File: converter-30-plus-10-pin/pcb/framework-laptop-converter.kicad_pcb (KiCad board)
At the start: 4 copper layers, 17.9 x 38 mm, 7 parts, among them J1 20879-040E-01, J2 FFC2B28-40-G

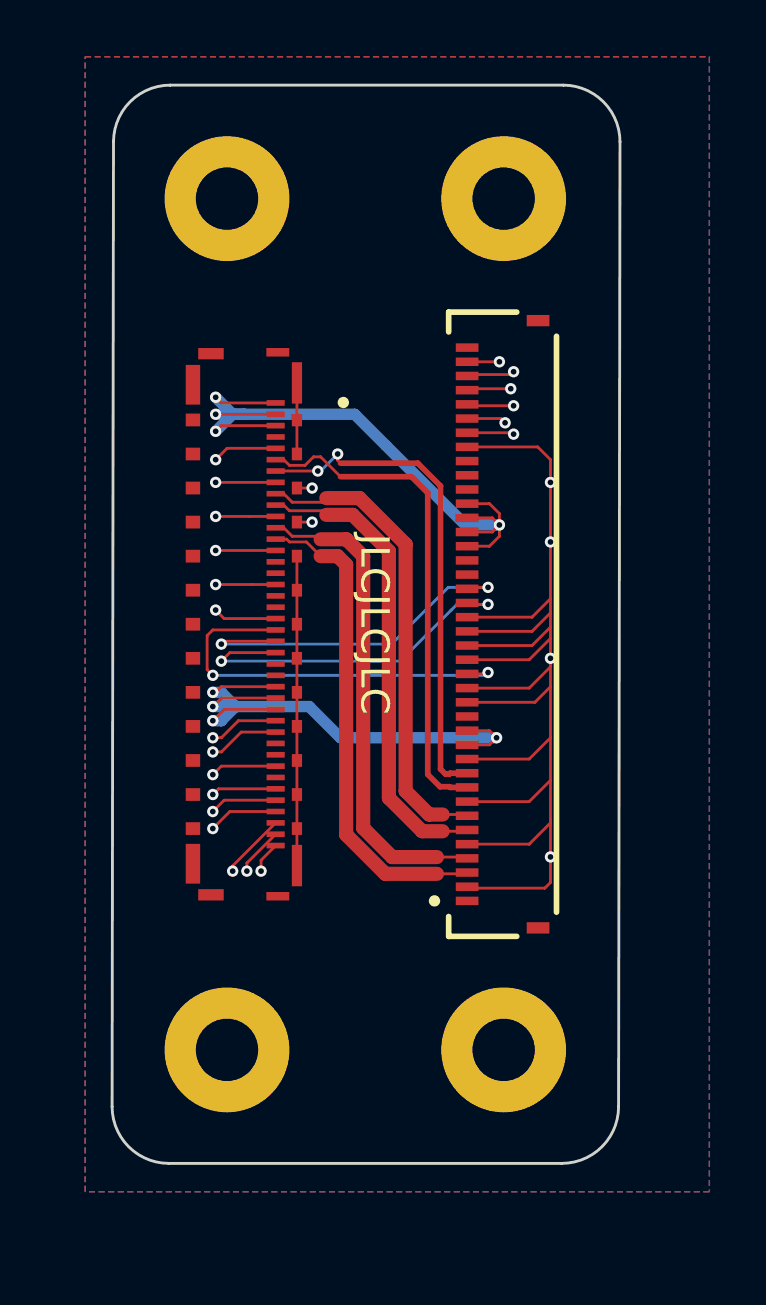
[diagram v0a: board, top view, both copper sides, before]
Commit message: fewer slots so this can be fabbed cheaper
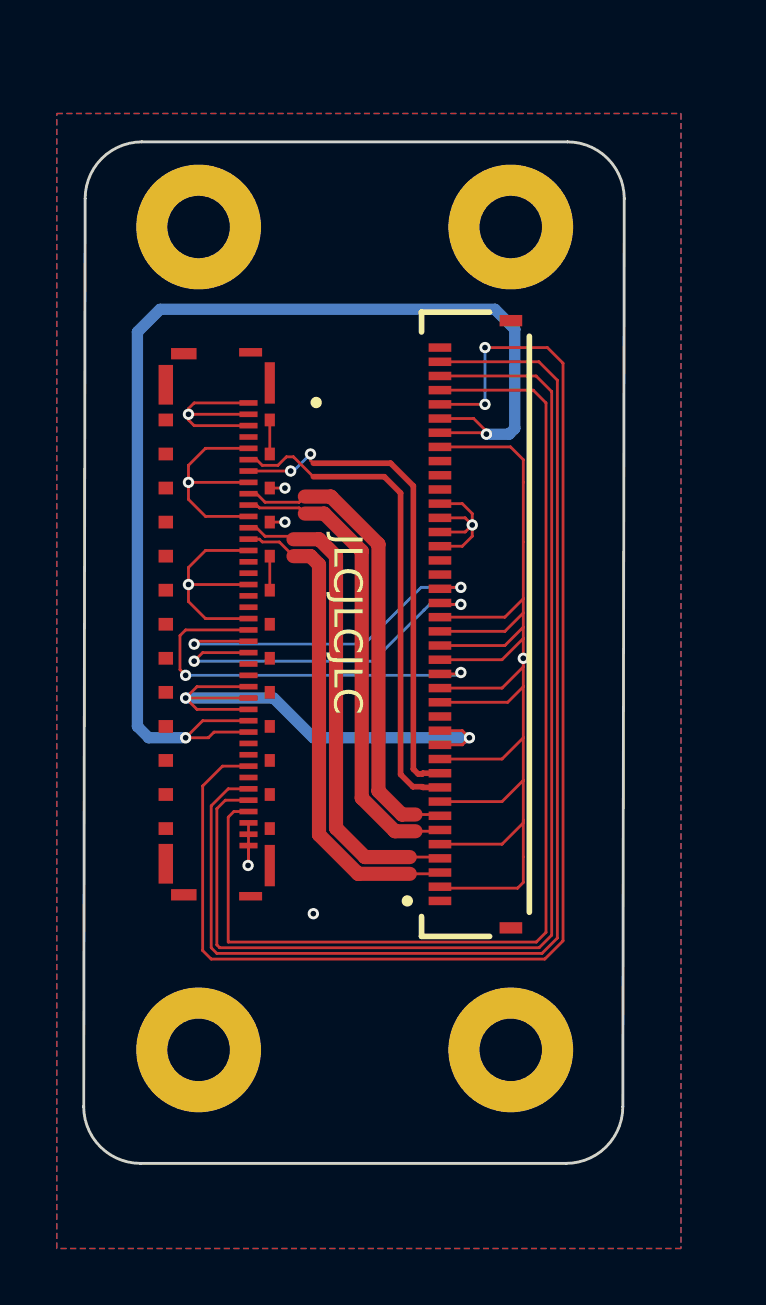
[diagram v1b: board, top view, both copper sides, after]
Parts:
- moved H1 1.41 mm to (137.0, 85.0)
- moved H2 1.03 mm to (148.0, 85.0)
- moved H3 1.00 mm to (137.0, 114.0)
- moved J2 0.96 mm to (146.8, 99.0)
- moved J1 0.96 mm to (137.7, 99.0)
- moved H4 0.25 mm to (148.0, 114.0)
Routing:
- net TS_EN: track 29.2 -> 47.7 mm
- net TS_INT_N: track 25.2 -> 43.1 mm, vias 2 -> 0
- net TS_SDA: track 26.4 -> 41.4 mm, vias 2 -> 0
- net BL_PWR: track 26.0 -> 12.8 mm, vias 4 -> 2
- net TS_SCL: track 26.2 -> 39.1 mm, vias 2 -> 0
- net SHIELD: track 14.5 -> 3.47 mm, vias 2 -> 3
- net TS_3V: track 36.6 -> 42.6 mm, vias 4 -> 2
- net EDP_3V: track 21.8 -> 19.8 mm, vias 4 -> 2
- net BL_GND: track 68.3 -> 68.5 mm, vias 13 -> 4
- added copper zone on In2.Cu, net BL_PWR
- removed copper zone on In2.Cu, net BL_GND
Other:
- board size 17.9 x 38 mm -> 19.1 x 36 mm

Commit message: start migrating converter to framework's true pinout
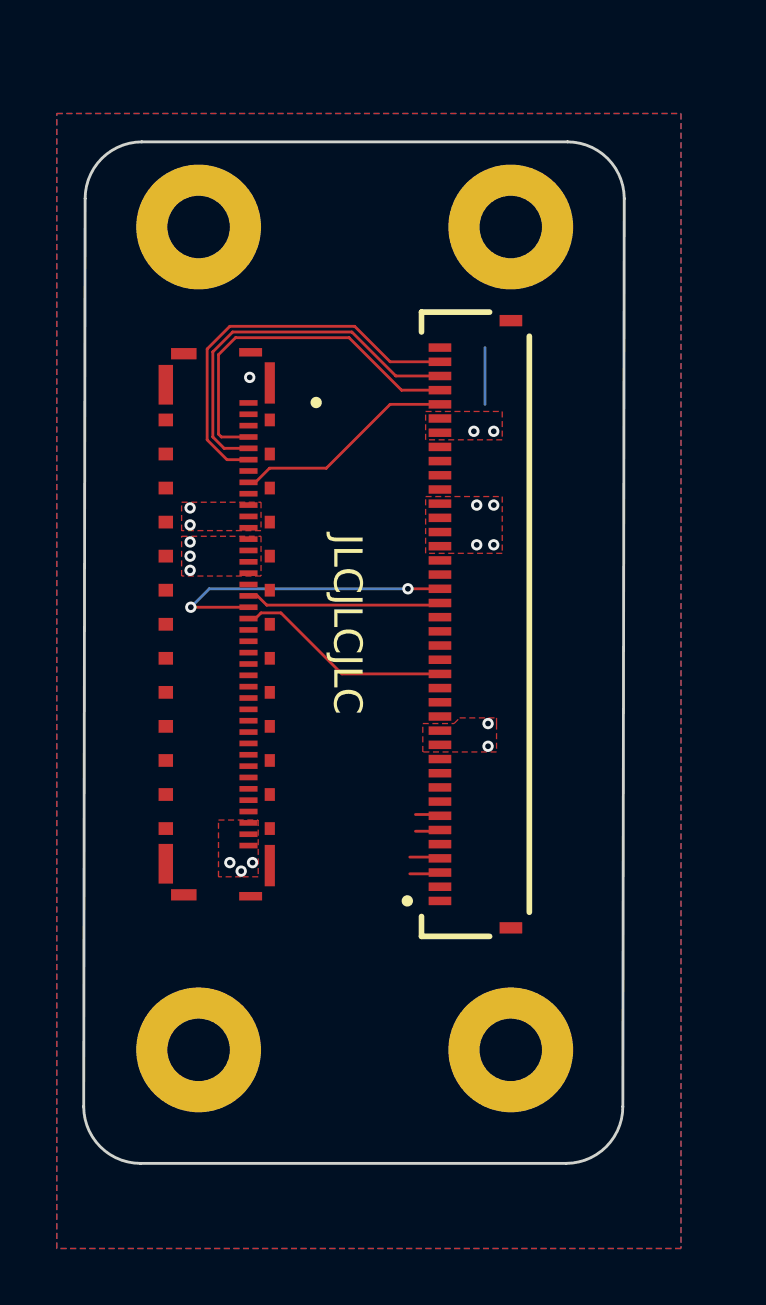
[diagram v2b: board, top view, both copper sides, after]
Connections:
- H1 pad 1: SHIELD -> GND
- H2 pad 1: SHIELD -> GND
- H3 pad 1: SHIELD -> GND
- H4 pad 1: SHIELD -> GND
- J1 pad 1: BL_PWR -> GND
- J1 pad 10: EDP_LANE0_N -> unconnected-(J1-Pad10)
- J1 pad 11: BL_GND -> TS_3V
- J1 pad 12: EDP_LANE1_P -> TS_3V
- J1 pad 13: EDP_LANE1_N -> EDP_3V
- J1 pad 14: BL_GND -> EDP_3V
- J1 pad 15: unconnected-(J1-Pad15) -> EDP_3V
- J1 pad 17: BL_GND -> unconnected-(J1-Pad17)
- J1 pad 18: unconnected-(J1-Pad18) -> BL_EN
- J1 pad 19: unconnected-(J1-Pad19) -> BL_PWM_DIM
- J1 pad 2: BL_PWR -> GND
- J1 pad 20: BL_GND -> EDP_HPD
- J1 pad 21: EDP_HPD -> GND
- J1 pad 22: BL_PWM_DIM -> unconnected-(J1-Pad22)
- J1 pad 23: BL_EN -> unconnected-(J1-Pad23)
- J1 pad 24: unconnected-(J1-Pad24) -> GND
- J1 pad 26: EDP_3V -> unconnected-(J1-Pad26)
- J1 pad 27: EDP_3V -> GND
- J1 pad 28: EDP_3V -> EDP_LANE1_N
- J1 pad 29: TS_3V -> EDP_LANE1_P
- J1 pad 3: BL_PWR -> GND
- J1 pad 30: TS_3V -> GND
- J1 pad 31: unconnected-(J1-Pad31) -> EDP_LANE0_N
- J1 pad 32: unconnected-(J1-Pad32) -> EDP_LANE0_P
- J1 pad 33: TS_EN -> GND
- J1 pad 34: unconnected-(J1-Pad34) -> EDP_AUX_N
- J1 pad 35: TS_INT_N -> EDP_AUX_P
- J1 pad 36: TS_SDA -> GND
- J1 pad 37: TS_SCL -> unconnected-(J1-Pad37)
- J1 pad 38: BL_GND -> BL_PWR
- J1 pad 39: BL_GND -> BL_PWR
- J1 pad 4: unconnected-(J1-Pad4) -> TS_SCL
- J1 pad 40: BL_GND -> BL_PWR
- J1 pad 5: BL_GND -> TS_SDA
- J1 pad 6: EDP_AUX_P -> TS_INT_N
- J1 pad 7: EDP_AUX_N -> unconnected-(J1-Pad7)
- J1 pad 8: BL_GND -> TS_EN
- J1 pad 9: EDP_LANE0_P -> unconnected-(J1-Pad9)
- J1 pad S1: SHIELD -> GND
- J1 pad S10: SHIELD -> GND
- J1 pad S11: SHIELD -> GND
- J1 pad S12: SHIELD -> GND
- J1 pad S13: SHIELD -> GND
- J1 pad S14: SHIELD -> GND
- J1 pad S15: SHIELD -> GND
- J1 pad S16: SHIELD -> GND
- J1 pad S17: SHIELD -> GND
- J1 pad S18: SHIELD -> GND
- J1 pad S19: SHIELD -> GND
- J1 pad S2: SHIELD -> GND
- J1 pad S20: SHIELD -> GND
- J1 pad S21: SHIELD -> GND
- J1 pad S22: SHIELD -> GND
- J1 pad S23: SHIELD -> GND
- J1 pad S24: SHIELD -> GND
- J1 pad S25: SHIELD -> GND
- J1 pad S26: SHIELD -> GND
- J1 pad S27: SHIELD -> GND
- J1 pad S28: SHIELD -> GND
- J1 pad S29: SHIELD -> GND
- J1 pad S3: SHIELD -> GND
- J1 pad S30: SHIELD -> GND
- J1 pad S31: SHIELD -> GND
- J1 pad S32: SHIELD -> GND
- J1 pad S33: SHIELD -> GND
- J1 pad S34: SHIELD -> GND
- J1 pad S4: SHIELD -> GND
- J1 pad S5: SHIELD -> GND
- J1 pad S6: SHIELD -> GND
- J1 pad S7: SHIELD -> GND
- J1 pad S8: SHIELD -> GND
- J1 pad S9: SHIELD -> GND
- J2 pad 11: BL_GND -> GND
- J2 pad 15: BL_GND -> GND
- J2 pad 16: BL_GND -> GND
- J2 pad 18: BL_GND -> GND
- J2 pad 19: BL_GND -> GND
- J2 pad 2: BL_GND -> GND
- J2 pad 20: BL_GND -> GND
- J2 pad 21: BL_GND -> GND
- J2 pad 33: BL_GND -> GND
- J2 pad 5: BL_GND -> GND
- J2 pad 8: BL_GND -> GND
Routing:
- net BL_GND: track 68.5 -> 0.00 mm, vias 4 -> 0
- net TS_3V: track 42.6 -> 0.00 mm, vias 2 -> 4
- net TS_EN: track 47.7 -> 9.89 mm, vias 2 -> 0
- net TS_INT_N: track 43.1 -> 14.0 mm
- net TS_SDA: track 41.4 -> 13.4 mm
- net TS_SCL: track 39.1 -> 12.7 mm
- net EDP_3V: track 19.8 -> 0.00 mm, vias 2 -> 5
- net EDP_AUX_N: track 17.7 -> 0.00 mm, vias 2 -> 0
- net EDP_AUX_P: track 17.6 -> 0.00 mm
- net EDP_LANE1_N: track 17.2 -> 1.08 mm
- net EDP_LANE1_P: track 17.2 -> 1.08 mm
- net EDP_LANE0_P: track 16.7 -> 0.88 mm
- net EDP_LANE0_N: track 16.6 -> 0.88 mm
- net BL_PWR: track 12.8 -> 0.00 mm, vias 2 -> 7
- net EDP_HPD: track 14.5 -> 7.72 mm, vias 2 -> 0
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- added copper zone on F.Cu, net BL_PWR
- added copper zone on F.Cu, net EDP_3V
- added copper zone on In2.Cu, net EDP_3V
- added copper zone on B.Cu, net GND
- added copper zone on F.Cu, net GND
- added copper zone on In1.Cu, net GND
- added copper zone on F.Cu, net TS_3V
- added copper zone on In2.Cu, net TS_3V
- removed copper zone on In1.Cu, net BL_GND
- removed copper zone on B.Cu, net SHIELD
- removed copper zone on F.Cu, net SHIELD

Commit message: converter: route edp lane 0 and aux + fix shield to ground
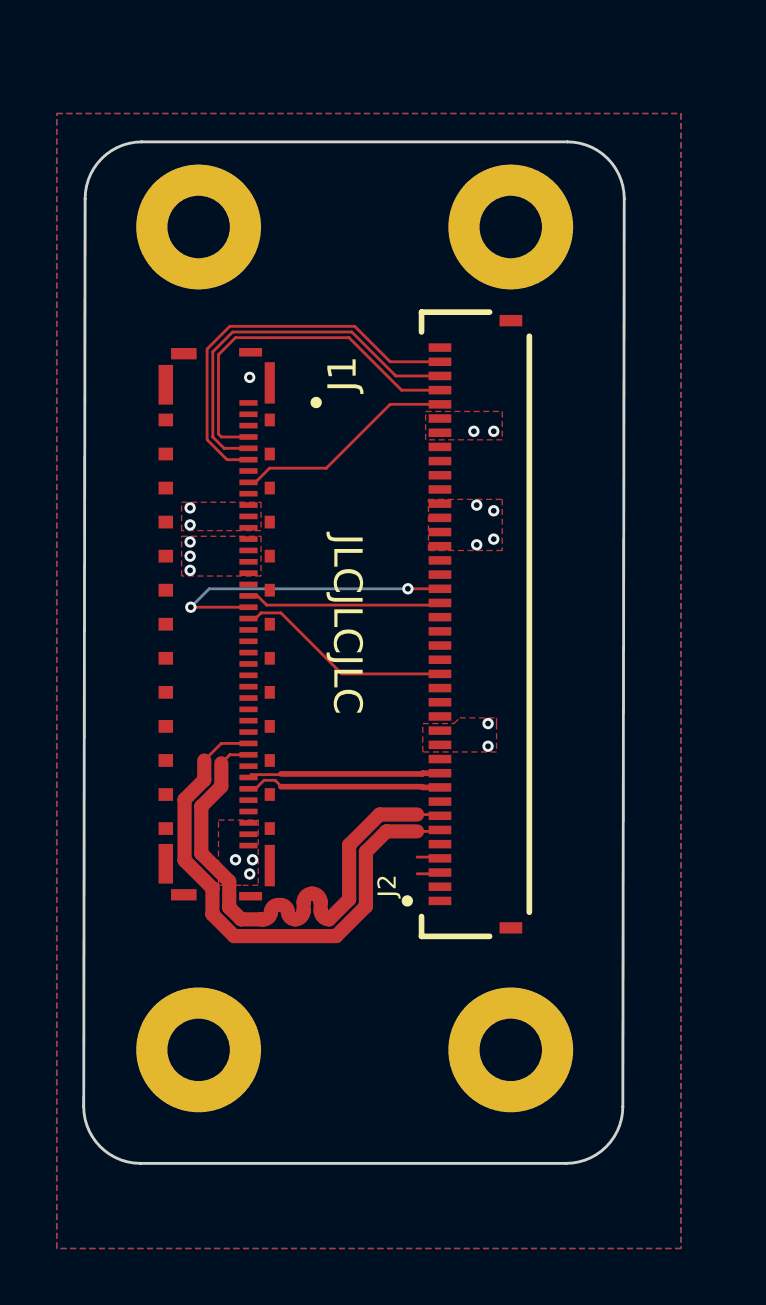
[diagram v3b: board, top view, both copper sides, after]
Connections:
- J2 pad S1: SHIELD -> GND
- J2 pad S2: SHIELD -> GND
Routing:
- net EDP_LANE0_N: track 0.88 -> 18.9 mm
- net EDP_LANE0_P: track 0.88 -> 18.9 mm
- net EDP_AUX_P: track 0.00 -> 6.96 mm
- net EDP_AUX_N: track 0.00 -> 6.80 mm
- net TS_EN: track 9.89 -> 7.89 mm
